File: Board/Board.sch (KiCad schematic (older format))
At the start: 7 parts

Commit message: Schematic: 7segment display done
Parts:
- removed D?: VQE23, symbol VQE23
- removed RN?: R_Pack07, symbol R_Pack07
- removed U?: 74LS48, symbol 74LS48
- added C? (x2): 100n, Capacitors_SMD:C_0603_HandSoldering, symbol C
- added D?: VQE24, symbol VQE24
- added R? (x16): 39R, Resistors_SMD:R_0603_HandSoldering, symbol R
- added R? (x2): 10k, symbol R
- added R? (x2): 10k, Resistors_SMD:R_0603_HandSoldering, symbol R
- added U? (x2): PCA9551, SMD_Packages:SO-16-N, symbol PCA9551
- C?: footprint (none) -> Capacitors_SMD:C_0603_HandSoldering
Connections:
- net labels added: a1, a2, b1, b2, c1, c2, d1, d2, e1, e2, f1, f2, g1, g2, h1, h2
- net labels removed: A, B, C, D
- wire segments 82 -> 130
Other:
- moved on the sheet: C?, P?, U?

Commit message: Power supply
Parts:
- added C? (x2): 0.1µ, symbol C
- added J?: Screw_Terminal_1x02, n39-kicad:AKL_101-02, symbol Screw_Terminal_1x02
- added P?: USB_B, Connect:USB_Micro-B, symbol USB_B
- added U?: LM1117-3.3, TO_SOT_Packages_SMD:SOT-223, symbol LM1117-3.3
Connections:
- net GND: now also C?.2, C?.2, J?.2, P?.4 (GND), U?.1 (GND/ADJ)
- net VCC: now also U?.2 (VO), U?.4 (VO)
- net VDD: now also C?.1, J?.1, P?.1 (VBUS), U?.3 (VI)
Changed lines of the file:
@@
 	7200 3150 6750 3150
 Wire Wire Line
-	10100 4500 10100 4600
-Wire Wire Line
-	10100 4600 10100 4950
-Wire Wire Line
-	10100 5250 10100 5650
-Wire Wire Line
-	10100 5650 10100 5750
+	10100 4500 10100 4950
+Wire Wire Line
+	10100 5250 10100 5750
 Wire Wire Line
 	8400 4950 8600 4950
@@
 	9600 5050 9750 5050
 Wire Wire Line
-	9750 5050 9750 5150
-Wire Wire Line
-	9750 5150 9750 5250
-Wire Wire Line
-	9750 5250 9750 5650
+	9750 5050 9750 5650
 Wire Wire Line
 	9600 5150 9750 5150
@@
 	2000 4750 2000 4650
 Wire Wire Line
-	2000 4650 2100 4650
-Wire Wire Line
-	2100 4650 2200 4650
-Wire Wire Line
-	2200 4650 2400 4650
+	2000 4650 2400 4650
 Wire Wire Line
 	2400 4650 2400 4750
@@
 	1450 5750 950  5750
 Wire Wire Line
-	950  5550 950  5750
-Wire Wire Line
-	950  5750 950  5850
+	950  5550 950  5850
 Wire Wire Line
 	1400 5150 1450 5150
@@
 	1450 5050 950  5050
 Wire Wire Line
-	950  4950 950  5050
-Wire Wire Line
-	950  5050 950  5150
-Wire Wire Line
-	950  5150 950  5250
+	950  4950 950  5250
 Connection ~ 950  5050
 Connection ~ 950  5750
@@
 Connection ~ 950  5150
 Wire Wire Line
-	2100 6200 2200 6200
-Wire Wire Line
-	2200 6200 2400 6200
+	2100 6200 2400 6200
 Wire Wire Line
 	2400 6200 2400 6300
@@
 	1450 7300 950  7300
 Wire Wire Line
-	950  7100 950  7300
-Wire Wire Line
-	950  7300 950  7400
+	950  7100 950  7400
 Wire Wire Line
 	1400 6700 1450 6700
@@
 	1450 6600 950  6600
 Wire Wire Line
-	950  6500 950  6600
-Wire Wire Line
-	950  6600 950  6700
-Wire Wire Line
-	950  6700 950  6800
+	950  6500 950  6800
 Connection ~ 950  6600
 Connection ~ 950  7300
@@
 	4500 6150 4500 6250
 Wire Wire Line
-	4500 6250 5200 6250
-Wire Wire Line
-	5200 6250 6100 6250
+	4500 6250 6100 6250
 Wire Wire Line
 	6100 6250 6100 6150
@@
 Connection ~ 5200 6250
 Wire Wire Line
-	10050 3200 10400 3200
-Wire Wire Line
-	10400 3200 10600 3200
+	10050 3200 10600 3200
 Connection ~ 10400 3200
 Wire Wire Line
-	10050 3600 10250 3600
-Wire Wire Line
-	10250 3600 10600 3600
+	10050 3600 10600 3600
 Connection ~ 10250 3600
 Wire Wire Line
-	10250 2700 10250 2800
-Wire Wire Line
-	10250 2800 10250 3300
+	10250 2700 10250 3300
 Wire Wire Line
 	10250 2800 10400 2800
@@
 Connection ~ 10100 4600
 Wire Wire Line
-	9100 5650 9750 5650
-Wire Wire Line
-	9750 5650 10100 5650
+	9100 5650 10100 5650
 Connection ~ 10100 5650
 Connection ~ 9750 5650
+$Comp
+L Screw_Terminal_1x02 J?
+U 1 1 5AD3EFB6
+P 1100 1100
+F 0 "J?" H 1100 1350 50  0000 C TNN
+F 1 "Screw_Terminal_1x02" V 950 1100 50  0000 C TNN
+F 2 "n39-kicad:AKL_101-02" H 1100 875 50  0001 C CNN
+F 3 "" H 1075 1100 50  0001 C CNN
+	1    1100 1100
+	1    0    0    -1
+$EndComp
+$Comp
+L USB_B P?
+U 1 1 5AD3F1CE
+P 1200 2100
+F 0 "P?" H 1400 1900 50  0000 C CNN
+F 1 "USB_B" H 1150 2300 50  0000 C CNN
+F 2 "Connect:USB_Micro-B" V 1150 2000 50  0001 C CNN
+F 3 "" V 1150 2000 50  0000 C CNN
+	1    1200 2100
+	0    -1   1    0
+$EndComp
+$Comp
+L GND #PWR?
+U 1 1 5AD3FEC4
+P 1650 2300
+F 0 "#PWR?" H 1650 2050 50  0001 C CNN
+F 1 "GND" H 1650 2150 50  0000 C CNN
+F 2 "" H 1650 2300 50  0000 C CNN
+F 3 "" H 1650 2300 50  0000 C CNN
+	1    1650 2300
+	1    0    0    -1
+$EndComp
+Wire Wire Line
+	1500 2200 1650 2200
+Wire Wire Line
+	1650 2200 1650 2300
+Wire Wire Line
+	1500 1900 1650 1900
+Wire Wire Line
+	1650 1900 1650 1800
+$Comp
+L GND #PWR?
+U 1 1 5AD40223
+P 1650 1300
+F 0 "#PWR?" H 1650 1050 50  0001 C CNN
+F 1 "GND" H 1650 1150 50  0000 C CNN
+F 2 "" H 1650 1300 50  0000 C CNN
+F 3 "" H 1650 1300 50  0000 C CNN
+	1    1650 1300
+	1    0    0    -1
+$EndComp
+Wire Wire Line
+	1300 1000 1650 1000
+Wire Wire Line
+	1650 1000 1650 900
+Wire Wire Line
+	1300 1200 1650 1200
+Wire Wire Line
+	1650 1200 1650 1300
+$Comp
+L VDD #PWR?
+U 1 1 5AD40ECC
+P 1650 900
+F 0 "#PWR?" H 1650 750 50  0001 C CNN
+F 1 "VDD" H 1650 1050 50  0000 C CNN
+F 2 "" H 1650 900 50  0000 C CNN
+F 3 "" H 1650 900 50  0000 C CNN
+	1    1650 900
+	1    0    0    -1
+$EndComp
+$Comp
+L VDD #PWR?
+U 1 1 5AD411EA
+P 1650 1800
+F 0 "#PWR?" H 1650 1650 50  0001 C CNN
+F 1 "VDD" H 1650 1950 50  0000 C CNN
+F 2 "" H 1650 1800 50  0000 C CNN
+F 3 "" H 1650 1800 50  0000 C CNN
+	1    1650 1800
+	1    0    0    -1
+$EndComp
+$Comp
+L VDD #PWR?
+U 1 1 5AD4147C
+P 2500 950
+F 0 "#PWR?" H 2500 800 50  0001 C CNN
+F 1 "VDD" H 2500 1100 50  0000 C CNN
+F 2 "" H 2500 950 50  0000 C CNN
+F 3 "" H 2500 950 50  0000 C CNN
+	1    2500 950
+	1    0    0    -1
+$EndComp
+$Comp
+L GND #PWR?
+U 1 1 5AD414E4
+P 2500 1550
+F 0 "#PWR?" H 2500 1300 50  0001 C CNN
+F 1 "GND" H 2500 1400 50  0000 C CNN
+F 2 "" H 2500 1550 50  0000 C CNN
+F 3 "" H 2500 1550 50  0000 C CNN
+	1    2500 1550
+	1    0    0    -1
+$EndComp
+Wire Wire Line
+	2500 950  2500 1050
+Wire Wire Line
+	2500 1050 3000 1050
+Wire Wire Line
+	2500 1550 2500 1450
+Wire Wire Line
+	2500 1450 3800 1450
+Wire Wire Line
+	3300 1450 3300 1350
+$Comp
+L C C?
+U 1 1 5AD419E3
+P 2750 1250
+F 0 "C?" H 2775 1350 50  0000 L CNN
+F 1 "0.1µ" H 2775 1150 50  0000 L CNN
+F 2 "" H 2788 1100 50  0000 C CNN
+F 3 "" H 2750 1250 50  0000 C CNN
+	1    2750 1250
+	1    0    0    -1
+$EndComp
+Wire Wire Line
+	2750 1100 2750 1050
+Connection ~ 2750 1050
+Wire Wire Line
+	2750 1400 2750 1450
+Connection ~ 2750 1450
+$Comp
+L VCC #PWR?
+U 1 1 5AD41DB7
+P 4200 950
+F 0 "#PWR?" H 4200 800 50  0001 C CNN
+F 1 "VCC" H 4200 1100 50  0000 C CNN
+F 2 "" H 4200 950 50  0000 C CNN
+F 3 "" H 4200 950 50  0000 C CNN
+	1    4200 950
+	1    0    0    -1
+$EndComp
+Wire Wire Line
+	3600 1050 4200 1050
+Wire Wire Line
+	4200 1050 4200 950
+$Comp
+L C C?
+U 1 1 5AD41FA2
+P 3800 1200
+F 0 "C?" H 3825 1300 50  0000 L CNN
+F 1 "0.1µ" H 3825 1100 50  0000 L CNN
+F 2 "" H 3838 1050 50  0000 C CNN
+F 3 "" H 3800 1200 50  0000 C CNN
+	1    3800 1200
+	1    0    0    -1
+$EndComp
+Wire Wire Line
+	3800 1450 3800 1350
+Connection ~ 3300 1450
+$Comp
+L LM1117-3.3 U?
+U 1 1 5AD42652
+P 3300 1050
+F 0 "U?" H 3400 800 50  0000 C CNN
+F 1 "LM1117-3.3" H 3300 1300 50  0000 C CNN
+F 2 "TO_SOT_Packages_SMD:SOT-223" H 3300 1050 50  0001 C CNN
+F 3 "" H 3300 1050 50  0000 C CNN
+	1    3300 1050
+	1    0    0    -1
+$EndComp
 $EndSCHEMATC

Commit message: Power and ESP environment
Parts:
- added C?: 100µ, symbol C
- added D?: gn, LEDs:LED_0603, symbol LED
- added R?: R, Resistors_SMD:R_0603_HandSoldering, symbol R
- added R? (x5): 10k, Resistors_SMD:R_0603_HandSoldering, symbol R
- added R? (x2): 330R, Resistors_SMD:R_0603_HandSoldering, symbol R
- C? (x2): footprint (none) -> Capacitors_SMD:C_0603_HandSoldering
- U?: footprint (none) -> ESP8266:ESP-12E
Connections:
- net Alert: now also U?.5 (GPIO14); no longer U?.10 (GPIO15)
- net GND: now also C?.2, R?.1, R?.2; no longer U?.9 (GND)
- net SCL: now also R?.1, R?.2
- net SDA: now also R?.1, R?.2; no longer R?.2
- net VCC: now also C?.1, D?.2 (A), R?.1, R?.1, R?.2, R?.2
- net VDD: now also C?.1
- net RESET: now reaches U?.1 (REST)
- net RESET: now also U?.4 (GPIO16), R?.1
- net at U?.11 (GPIO2): now also R?.2
- net PROG: now reaches U?.12 (GPIO0)
- net PROG: now also R?.2
- net RX: now reaches U?.15 (RXD)
- net RX: now also P?.1 (P1); no longer P?.3 (P3)
- net TX: now reaches U?.16 (TXD)
- net TX: now also P?.3 (P3); no longer P?.1 (P1)
- net at U?.3 (CH_PD): now also R?.1
- net STATUS: now reaches U?.6 (GPIO12)
- new net: R?.2, U?.10 (GPIO15)
- new net: D?.1 (K), R?.1
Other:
- note added: "I2C address 0x18"
- note added: "I2C address 0x60"
- note added: "I2C address 0x61"
- moved on the sheet: C?, D?, P?, R?, U?

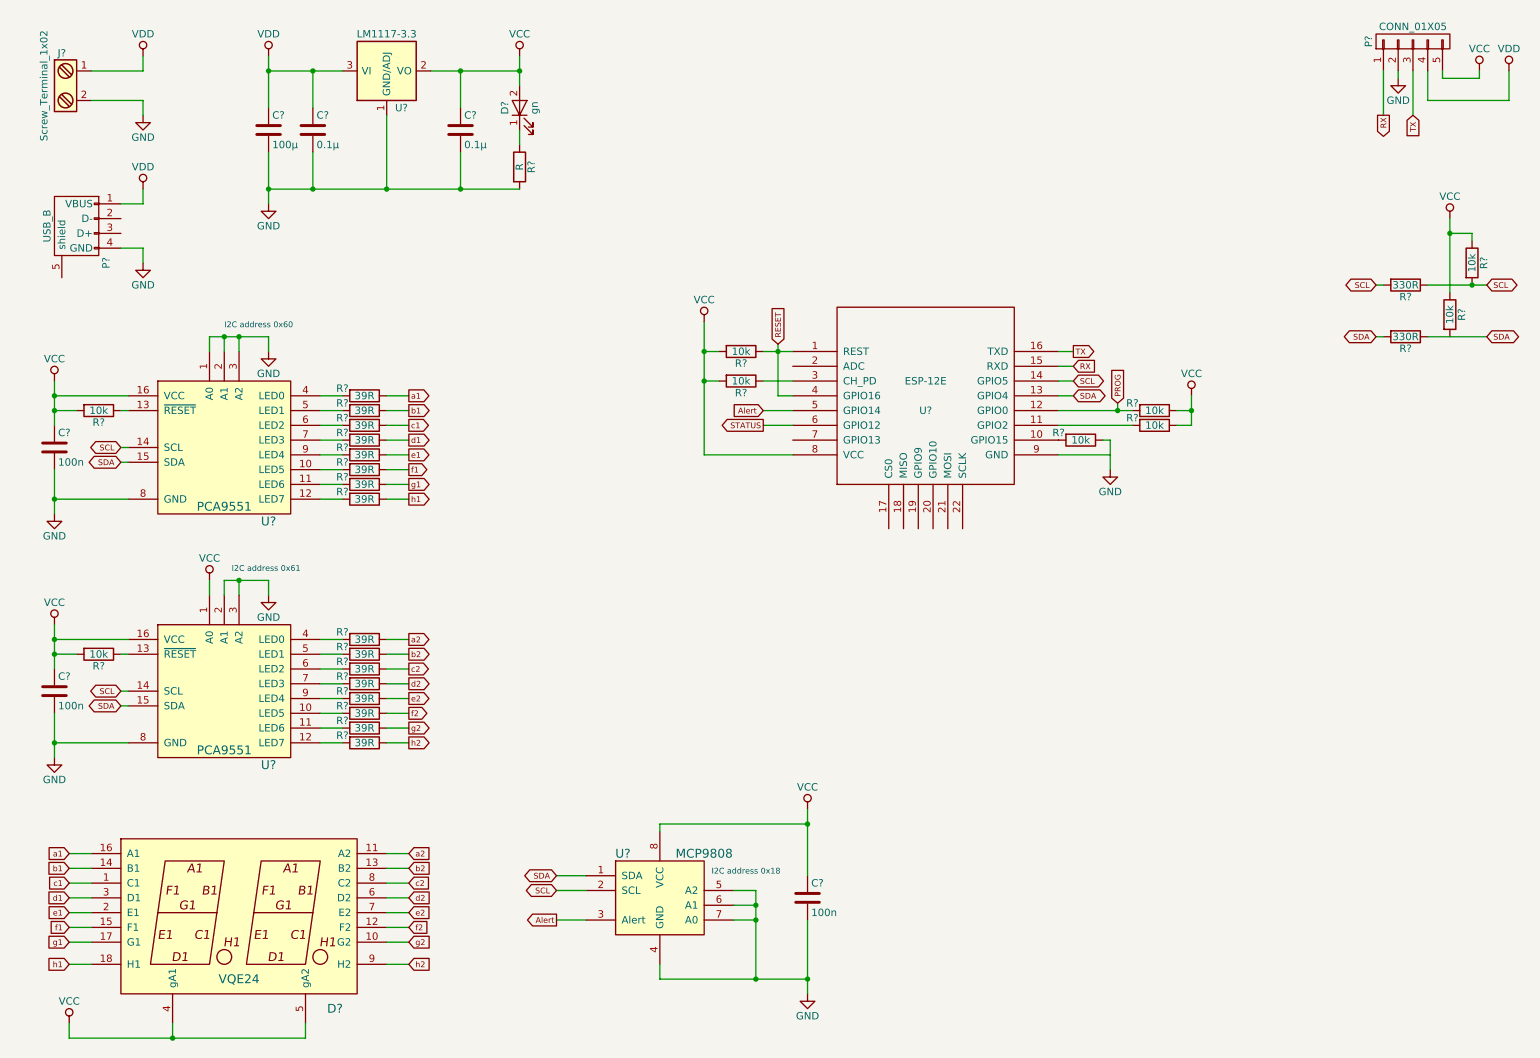
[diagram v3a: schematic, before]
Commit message: Use MCP23016
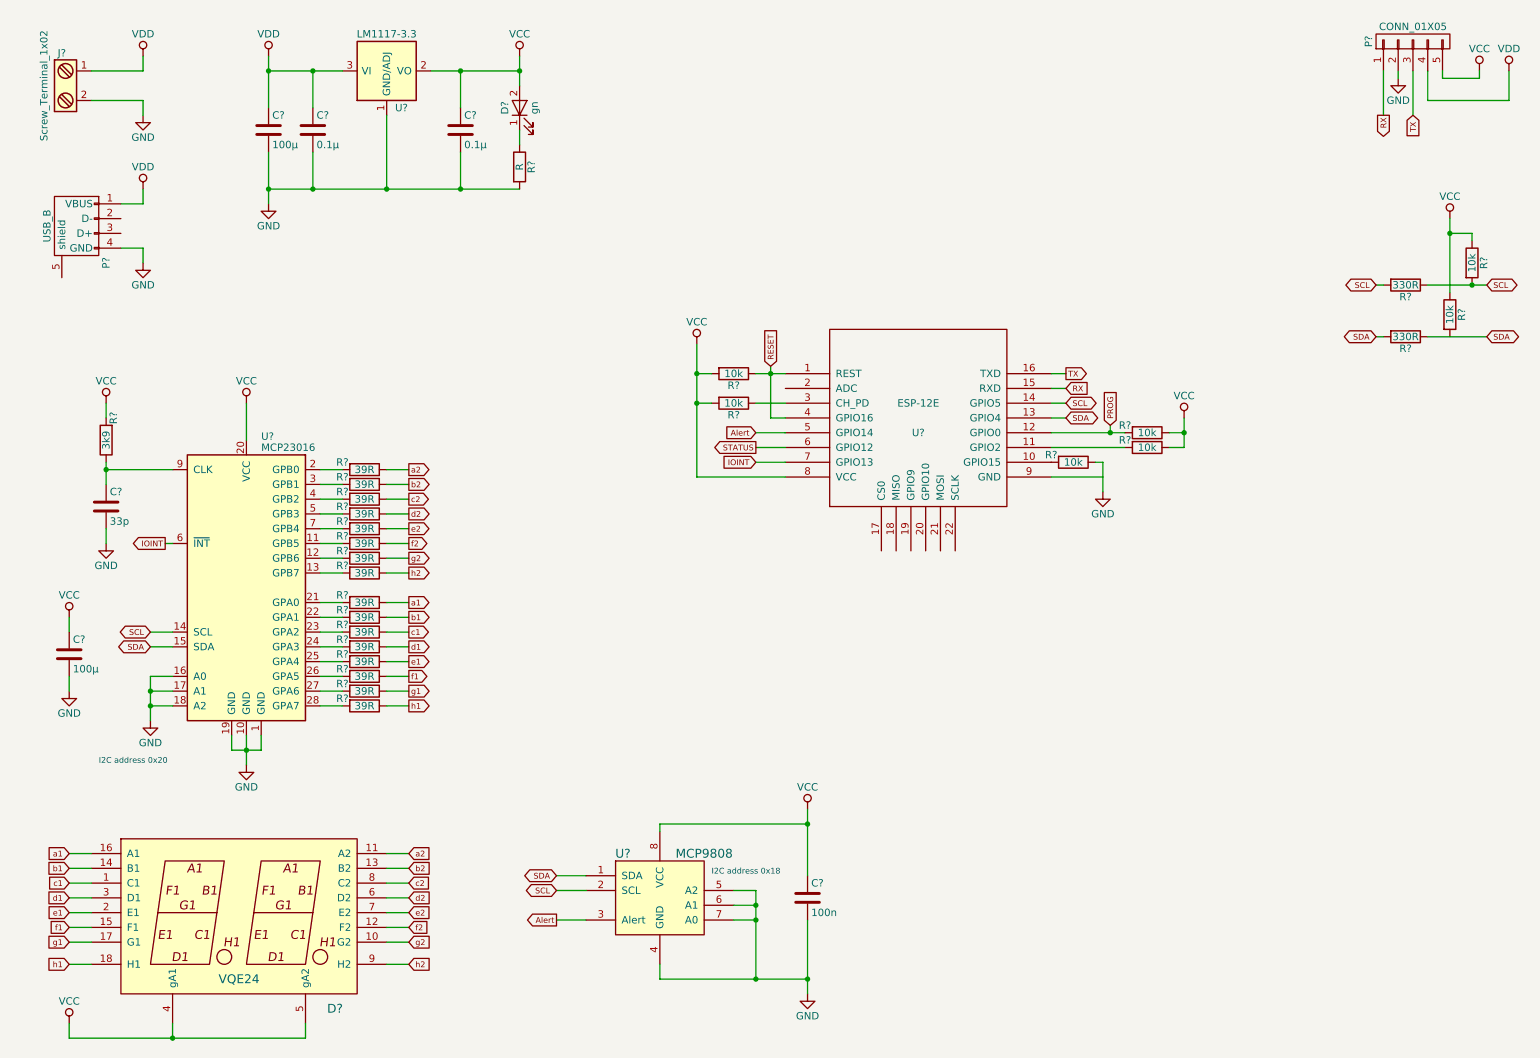
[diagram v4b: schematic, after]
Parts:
- removed C? (x2): 100n, Capacitors_SMD:C_0603_HandSoldering, symbol C
- removed R? (x2): 10k, symbol R
- removed U? (x2): PCA9551, SMD_Packages:SO-16-N, symbol PCA9551
- added C?: 33p, symbol C
- added C?: 100µ, symbol C
- added R?: 3k9, Resistors_SMD:R_0603_HandSoldering, symbol R
- added U?: MCP23016, SMD_Packages:SOIC-28, symbol MCP23016
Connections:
- net GND: now also C?.2, C?.2, U?.1 (GND), U?.10 (TP), U?.16 (A0), U?.17 (A1), U?.18 (A2), U?.19 (GND)
- net SCL: now also U?.14 (SCL)
- net SDA: now also U?.15 (SDA)
- net VCC: now also C?.1, R?.2, U?.20 (VCC)
- net IOINT: now reaches U?.7 (GPIO13)
- net IOINT: now also U?.6 (~INT)
- net at R?.2: now also U?.26 (GPA5)
- net at R?.2: now also U?.27 (GPA6)
- net at R?.2: now also U?.28 (GPA7)
- net at R?.2: now also U?.21 (GPA0)
- net at R?.2: now also U?.22 (GPA1)
- net at R?.2: now also U?.23 (GPA2)
- net at R?.2: now also U?.24 (GPA3)
- net at R?.2: now also U?.25 (GPA4)
- net at R?.2: now also U?.11 (GPB5)
- net at R?.2: now also U?.12 (GPB6)
- net at R?.2: now also U?.13 (GPB7)
- net at R?.2: now also U?.2 (GPB0)
- net at R?.2: now also U?.3 (GPB1)
- net at R?.2: now also U?.4 (GPB2)
- net at R?.2: now also U?.5 (GPB3)
- net at R?.2: now also U?.7 (GPB4)
- new net: C?.1, R?.1, U?.9 (CLK)
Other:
- note added: "I2C address 0x20"
- note removed: "I2C address 0x60"
- note removed: "I2C address 0x61"
- moved on the sheet: R?, U?
